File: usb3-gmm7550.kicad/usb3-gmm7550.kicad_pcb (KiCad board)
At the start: 4 copper layers, 75 x 50 mm, 205 parts, among them J1 USB_C_Receptacle, J2 USB_C_Receptacle_USB2.0, J3 SWD, J4 10144517-061802LF, J5 10144517-061802LF, J6 DNI, Q1 NX6008NBK, Q2 NX6008NBK, Q3 NX6008NBK, Q4 STL9P3LLH6, Q5 STL9P3LLH6, Q6 STL9P3LLH6, SW1 SW_Push, SW2 SW_Push, SW3 SW_Push, SW4 SW_Push, SW5 SW_Push, SW6 SW_DIP_x02, U1 ECMF4-40A100N10, U10 74LVC1G07, U11 INA180A2, U12 AP7330, U13 AP7330, U14 MX25R1635FZU, U15 ECMF02-2AMX6, U16 LM4040DBZ-3, U17 RP2040, U18 STUSB1600, U19 LM66200DRLR, U2 ECMF4-40A100N10, U3 ECMF02-2AMX6, U4 AP7330, U5 TUSB542, U6 SN65LVDS4RSER, U7 USB3340, U8 STUSB03E, U9 SiP32510, Y1 445I23D12M00000

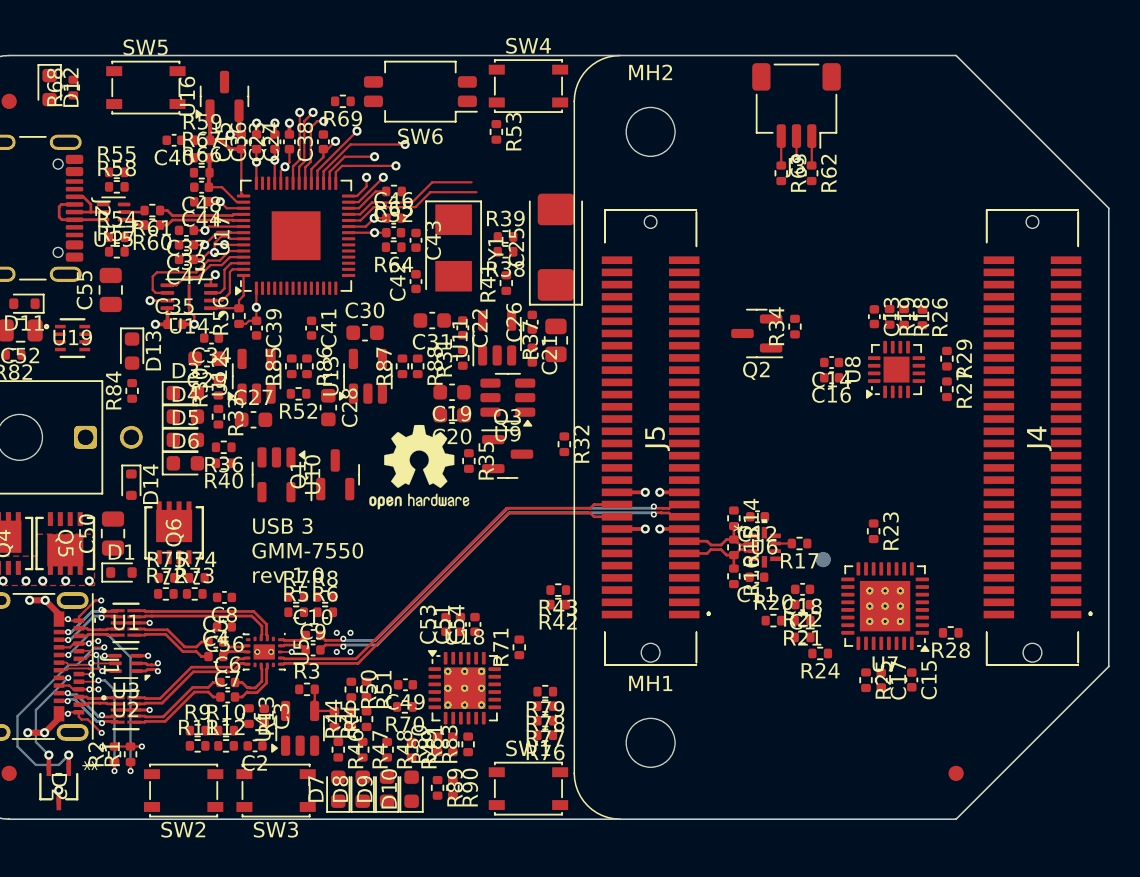
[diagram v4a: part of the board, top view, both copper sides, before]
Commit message: Layout -- suffling FPGA IOs (LEDs, buttons)
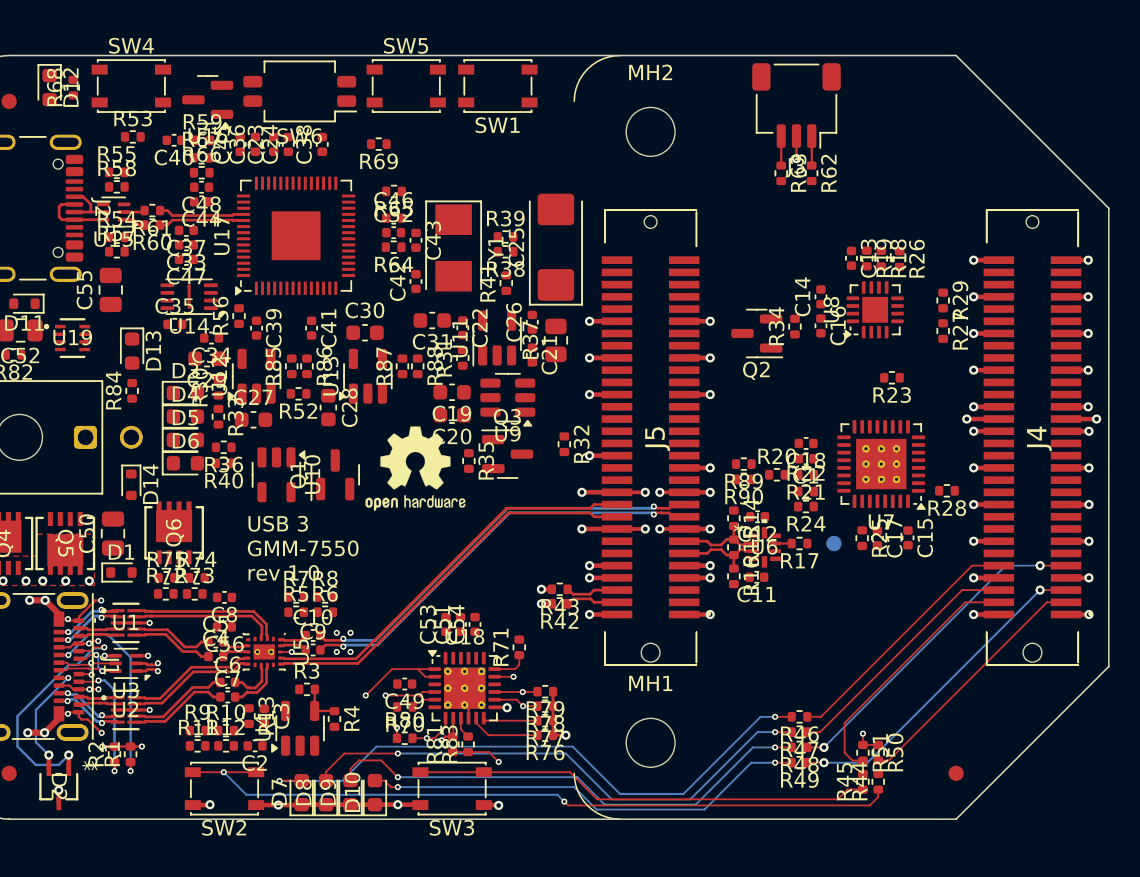
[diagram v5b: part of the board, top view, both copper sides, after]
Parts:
- moved SW1 46.0 mm to (95.0, 52.0), turned to 180 degrees
- moved R50 34.7 mm to (119.9, 95.7)
- moved R44 34.7 mm to (119.9, 97.5)
- moved R51 32.8 mm to (118.9, 95.7)
- moved R45 32.8 mm to (118.9, 97.5)
- moved R46 30.3 mm to (114.8, 93.3), turned to 180 degrees
- moved R89 29.2 mm to (111.1, 76.8), turned to 180 degrees
- moved R47 28.6 mm to (114.8, 94.3), turned to 180 degrees
- moved R90 27.8 mm to (111.1, 77.8), turned to 180 degrees
- moved R48 27.0 mm to (114.8, 95.3), turned to 180 degrees
- moved SW4 26.0 mm to (71.0, 52.0)
- moved R49 25.4 mm to (114.8, 96.3), turned to 180 degrees
- moved R53 23.8 mm to (71.1, 55.3), turned to 0 degrees
- moved SW5 17.1 mm to (89.0, 52.0)
- moved SW3 11.5 mm to (92.0, 98.0)
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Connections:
- J4 pad 10: ULPI_D7 -> /GMM-7550 IO/IO_SB_B2
- J4 pad 11: PD_RESET -> PD_SCL
- J4 pad 12: ULPI_D6 -> PD_SDA
- J4 pad 15: ULPI_D5 -> PD_ALERT_N
- J4 pad 16: ULPI_D3 -> unconnected-(J4-Pad16)
- J4 pad 17: ULPI_D4 -> unconnected-(J4-Pad17)
- J4 pad 18: ULPI_D2 -> unconnected-(J4-Pad18)
- J4 pad 28: PD_SCL -> unconnected-(J4-Pad28)
- J4 pad 3: ULPI_RST_N -> /GMM-7550 IO/IO_SB_B8
- J4 pad 30: PD_SDA -> unconnected-(J4-Pad30)
- J4 pad 38: PD_ALERT_N -> unconnected-(J4-Pad38)
- J4 pad 4: ULPI_NXT -> /GMM-7550 IO/IO_SB_B3
- J4 pad 49: /GMM-7550 IO/IO_SA_B2 -> unconnected-(J4-Pad49)
- J4 pad 5: ULPI_CLK -> /GMM-7550 IO/IO_SA_A8
- J4 pad 51: /GMM-7550 IO/IO_SA_A2 -> unconnected-(J4-Pad51)
- J4 pad 55: /GMM-7550 IO/IO_SA_B1 -> unconnected-(J4-Pad55)
- J4 pad 56: /GMM-7550 IO/IO_SA_B0 -> unconnected-(J4-Pad56)
- J4 pad 57: /GMM-7550 IO/IO_SA_A1 -> unconnected-(J4-Pad57)
- J4 pad 58: /GMM-7550 IO/IO_SA_A0 -> unconnected-(J4-Pad58)
- J4 pad 6: ULPI_DIR -> /GMM-7550 IO/IO_SB_A3
- J4 pad 9: ULPI_STP -> /GMM-7550 IO/IO_SB_B6
- R44 pad 2: /GMM-7550 IO/IO_SA_A2 -> /GMM-7550 IO/IO_SB_B8
- R45 pad 2: /GMM-7550 IO/IO_SA_B2 -> /GMM-7550 IO/IO_SB_B3
- R46 pad 1: /GMM-7550 IO/IO_SA_A0 -> /GMM-7550 IO/IO_SB_B2
- R47 pad 1: /GMM-7550 IO/IO_SA_A1 -> /GMM-7550 IO/IO_SB_A3
- R48 pad 1: /GMM-7550 IO/IO_SA_B0 -> /GMM-7550 IO/IO_SB_B6
- R49 pad 1: /GMM-7550 IO/IO_SA_B1 -> /GMM-7550 IO/IO_SA_A8
- R50 pad 2: /GMM-7550 IO/IO_SA_A2 -> /GMM-7550 IO/IO_SB_B8
- R51 pad 2: /GMM-7550 IO/IO_SA_B2 -> /GMM-7550 IO/IO_SB_B3
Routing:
- net GND: track 38.2 -> 103.2 mm, vias 30 -> 65
- net Net-(R44-Pad1): track 0.00 -> 48.6 mm, vias 0 -> 2
- net Net-(D7-A): track 0.00 -> 39.3 mm, vias 0 -> 2
- net Net-(D8-A): track 0.00 -> 34.6 mm, vias 0 -> 2
- net Net-(D9-A): track 0.00 -> 32.6 mm, vias 0 -> 2
- net Net-(R45-Pad1): track 0.00 -> 30.0 mm
- net Net-(D10-A): track 0.00 -> 29.3 mm, vias 0 -> 2
- net VIO_2V5: track 0.00 -> 23.2 mm, vias 0 -> 12
- net /GMM-7550 IO/IO_SB_B6: track 0.00 -> 21.9 mm, vias 0 -> 2
- net /GMM-7550 IO/IO_SA_A8: track 0.00 -> 21.6 mm, vias 0 -> 2
- net +2V5: track 17.2 -> 0.00 mm, vias 6 -> 0
- net /GMM-7550 IO/IO_SB_B3: track 0.00 -> 16.7 mm
- net /GMM-7550 IO/IO_SB_B2: track 0.00 -> 16.6 mm
- net /GMM-7550 IO/IO_SB_B8: track 0.00 -> 16.6 mm
- net /GMM-7550 IO/IO_SB_A3: track 0.00 -> 16.4 mm
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
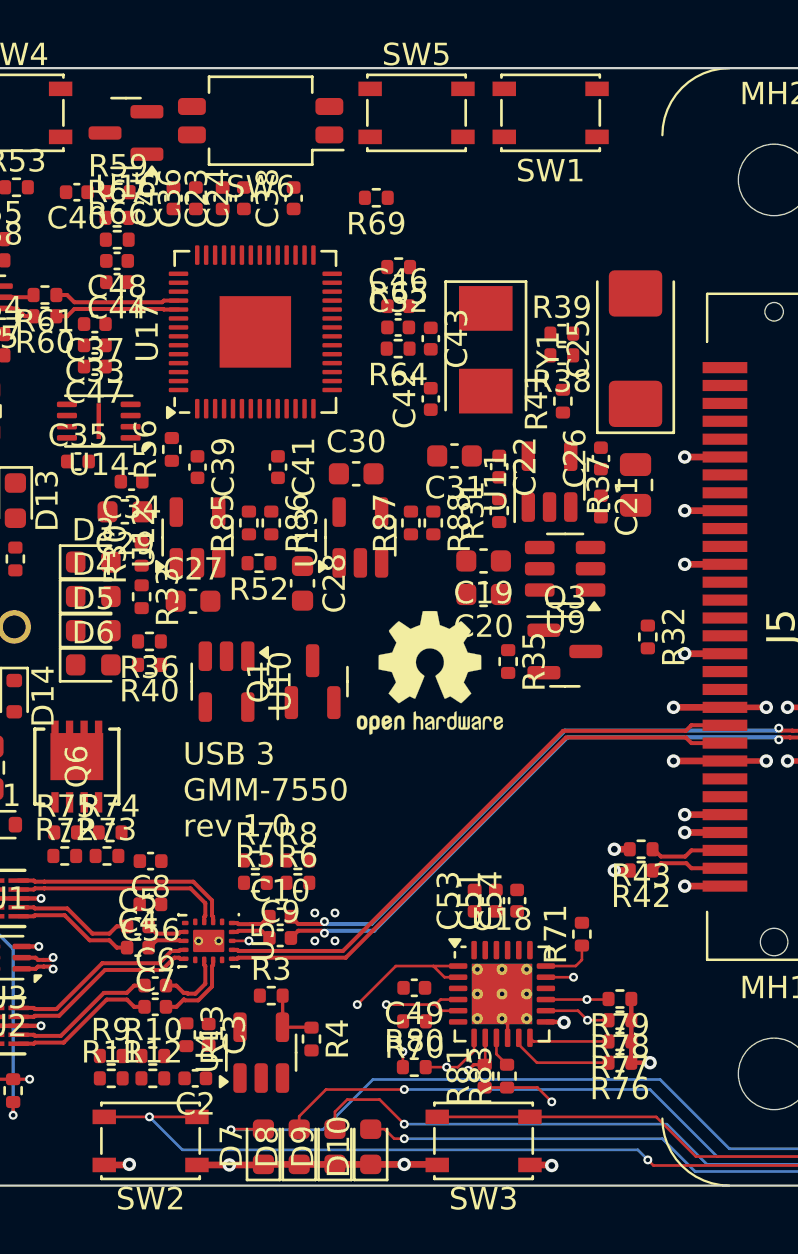
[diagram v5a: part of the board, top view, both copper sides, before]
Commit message: Add USB Type-C plug polarity indication (A_B_SIDE signal from PD controller)
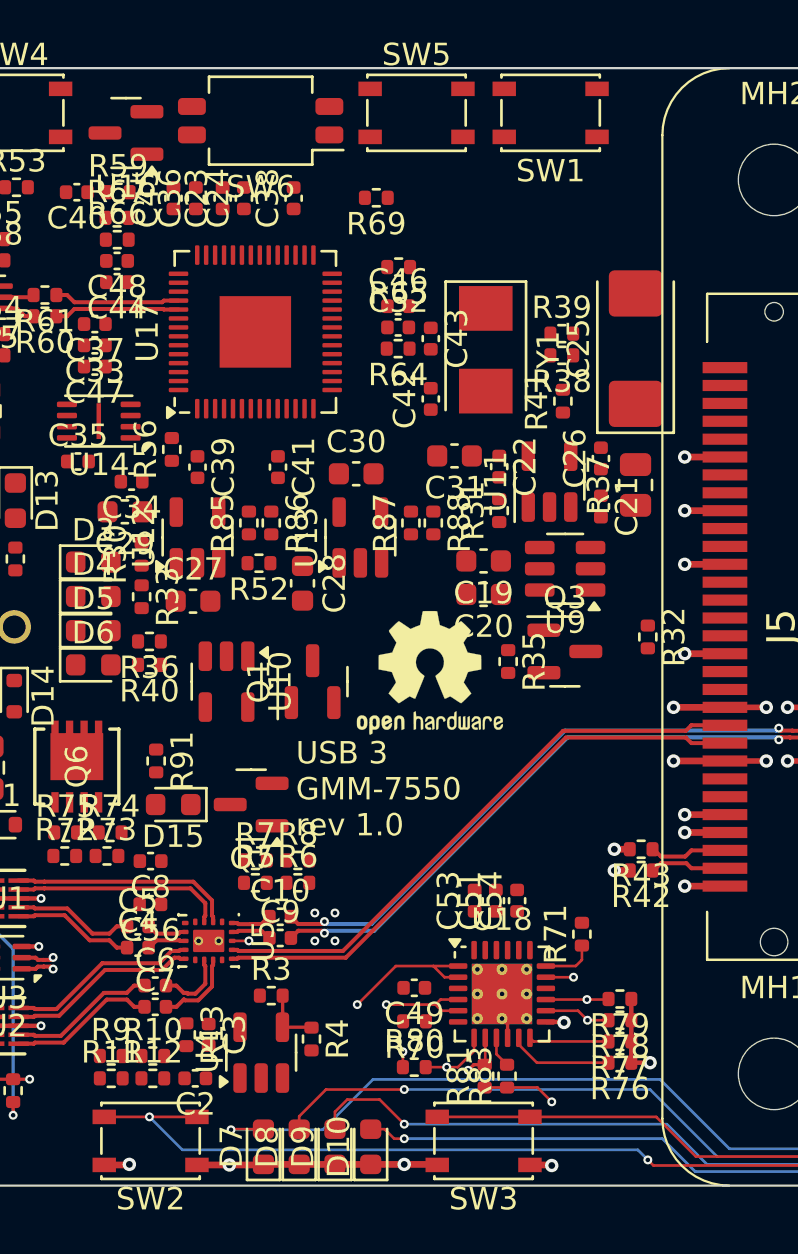
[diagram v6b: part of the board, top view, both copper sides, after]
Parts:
- added D15: HSMA-C197, LED_SMD:LED_0603_1608Metric, F.Cu at (78.1, 83.0)
- added Q7: NX6008NBK, Package_TO_SOT_SMD:SOT-23, F.Cu at (81.6, 83.0)
- added R91: 100, Resistor_SMD:R_0402_1005Metric, F.Cu at (77.3, 81.0)

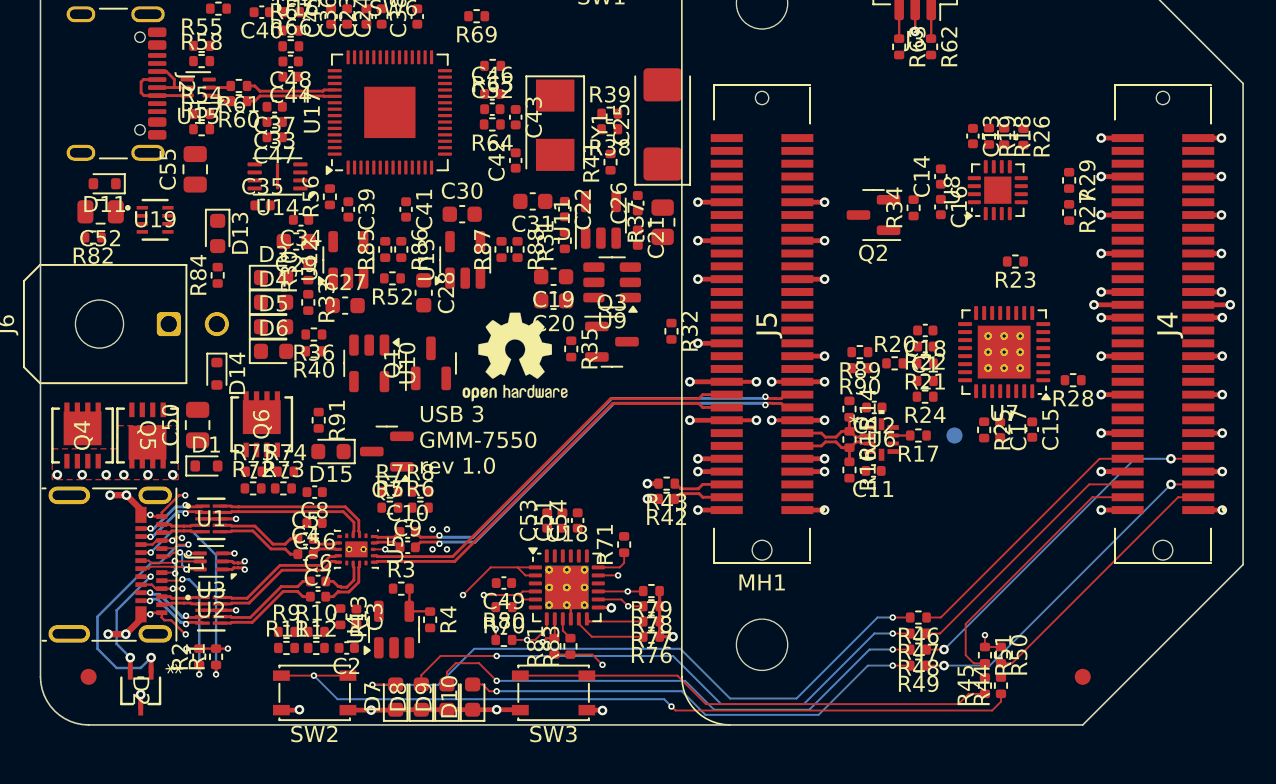
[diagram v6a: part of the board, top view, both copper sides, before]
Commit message: Layout -- re-arrange and connect all GMM-7550 IOs on J4 (USB 1.1 and 2.0)
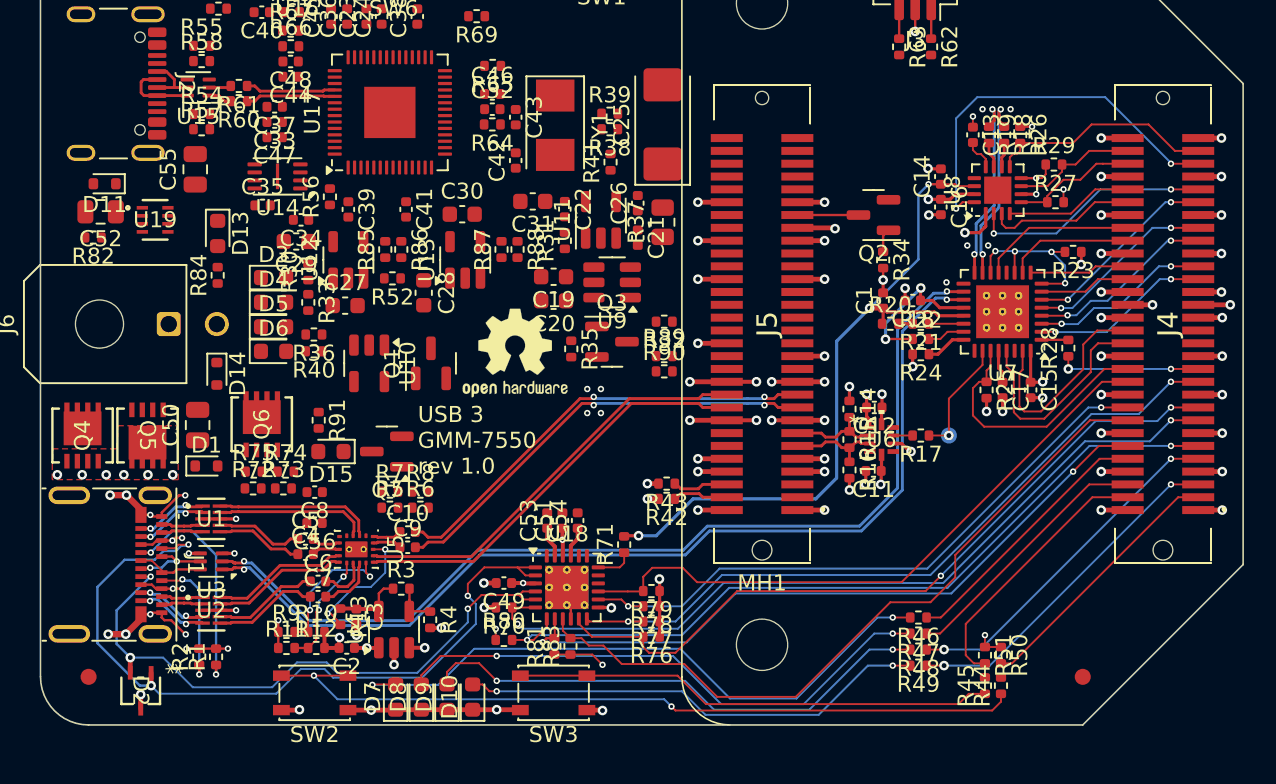
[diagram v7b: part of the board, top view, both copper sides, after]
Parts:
- moved R89 12.2 mm to (98.9, 77.0), turned to 0 degrees
- moved R90 12.2 mm to (98.9, 78.0), turned to 0 degrees
- moved C1 3.89 mm to (112.5, 73.5), turned to 90 degrees
- moved R34 3.76 mm to (112.5, 71.0), turned to -90 degrees
- moved R23 3.65 mm to (124.4, 70.5)
- moved R24 2.66 mm to (114.9, 76.9)
- moved R22 2.63 mm to (114.9, 75.9)
- moved U7 2.52 mm to (120.0, 74.2)
- moved C17 2.49 mm to (120.0, 79.1)
- moved R25 2.49 mm to (119.0, 79.1)
- moved R21 2.49 mm to (114.9, 75.0)
- moved R20 2.48 mm to (113.0, 75.0)
- moved C15 2.47 mm to (121.8, 79.1)
- moved C18 2.03 mm to (114.4, 73.5)
- moved R28 2.02 mm to (124.1, 76.5), turned to 90 degrees
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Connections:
- net /GMM-7550 IO/IO_SA_A8 renamed /GMM-7550 IO/IO_SB_A8
- J4 pad 15: PD_ALERT_N -> PD_RESET
- J4 pad 16: unconnected-(J4-Pad16) -> PD_ALERT_N
- J4 pad 17: unconnected-(J4-Pad17) -> PD_VBUS_VALID
- J4 pad 18: unconnected-(J4-Pad18) -> PD_DEBUG1
- J4 pad 21: IO_SB_B7 -> PD_ATTACH
- J4 pad 22: ULPI_D1 -> PD_DEBUG2
- J4 pad 23: IO_SB_A7 -> ULPI_CLK
- J4 pad 24: ULPI_D0 -> ULPI_RST_N
- J4 pad 27: PD_VBUS_VALID -> unconnected-(J4-Pad27)
- J4 pad 28: unconnected-(J4-Pad28) -> ULPI_STP
- J4 pad 29: PD_ATTACH -> unconnected-(J4-Pad29)
- J4 pad 30: unconnected-(J4-Pad30) -> ULPI_DIR
- J4 pad 37: USB1_BUSDET -> ULPI_NXT
- J4 pad 38: unconnected-(J4-Pad38) -> ULPI_D4
- J4 pad 39: USB1_CON -> ULPI_D0
- J4 pad 40: USB1_SUS -> ULPI_D5
- J4 pad 43: PD_DEBUG1 -> ULPI_D1
- J4 pad 44: USB1_VP -> ULPI_D6
- J4 pad 45: PD_DEBUG2 -> ULPI_D2
- J4 pad 46: USB1_VM -> ULPI_D7
- J4 pad 49: unconnected-(J4-Pad49) -> ULPI_D3
- J4 pad 50: USB1_OE_N -> USB1_VP
- J4 pad 51: unconnected-(J4-Pad51) -> USB1_RCV
- J4 pad 52: USB1_RCV -> USB1_VM
- J4 pad 55: unconnected-(J4-Pad55) -> USB1_BUSDET
- J4 pad 56: unconnected-(J4-Pad56) -> USB1_CON
- J4 pad 57: unconnected-(J4-Pad57) -> USB1_OE_N
- J4 pad 58: unconnected-(J4-Pad58) -> USB1_SUS
- U3 pad 1: USB2_D_P -> USB2_D_N
- U3 pad 2: USB2_D_N -> USB2_D_P
- U3 pad 5: /USB3/J1_D_N -> /USB3/J1_D_P
- U3 pad 6: /USB3/J1_D_P -> /USB3/J1_D_N
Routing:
- net USB2_D_P: track 1.49 -> 62.2 mm, vias 1 -> 2
- net USB2_D_N: track 1.49 -> 62.2 mm, vias 1 -> 2
- net PD_RESET: track 0.00 -> 50.6 mm, vias 0 -> 2
- net PD_SCL: track 3.05 -> 49.9 mm, vias 1 -> 2
- net VBUS_TRGT: track 5.46 -> 51.0 mm, vias 10 -> 13
- net PD_ALERT_N: track 1.40 -> 45.6 mm
- net PD_ATTACH: track 3.58 -> 45.3 mm, vias 0 -> 2
- net PD_VBUS_VALID: track 4.65 -> 46.4 mm, vias 0 -> 2
- net PD_SDA: track 2.06 -> 43.6 mm, vias 1 -> 2
- net PD_DEBUG2: track 2.85 -> 39.7 mm, vias 1 -> 0
- net PD_DEBUG1: track 2.98 -> 39.3 mm, vias 1 -> 2
- net CON_CC2: track 12.3 -> 38.5 mm
- net CON_CC1: track 22.9 -> 48.7 mm
- net USB1_BUSDET: track 0.00 -> 24.3 mm, vias 0 -> 2
- net GND: track 103.2 -> 124.4 mm, vias 65 -> 91
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
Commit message: Layout -- WIP...
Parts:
- added TP2: TestPoint, TestPoint:TestPoint_Pad_D1.0mm, B.Cu at (124.1, 77.8)
- moved C8 1.99 mm to (79.0, 84.9), turned to 0 degrees
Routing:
- net A_B_SIDE: track 8.01 -> 43.8 mm, vias 2 -> 4
- net GND: track 124.4 -> 150.9 mm, vias 91 -> 114
- net Net-(U18-VBUS_EN_SNK): track 0.00 -> 23.5 mm, vias 0 -> 2
- net Net-(U18-VBUS_EN_SRC): track 0.00 -> 23.2 mm, vias 0 -> 2
- net Net-(U11-+): track 0.00 -> 11.1 mm
- net VSW_1V8: track 6.36 -> 16.1 mm, vias 1 -> 5
- net /GMM-7550/VIN: track 0.00 -> 7.89 mm
- net Net-(U17-XIN): track 0.00 -> 7.73 mm
- net Net-(U5-CNFG_B1): track 0.00 -> 6.86 mm, vias 0 -> 2
- net VBUS_TRGT: track 51.0 -> 57.7 mm, vias 13 -> 15
- net +1V1: track 0.00 -> 6.52 mm
- net +5V: track 3.24 -> 9.60 mm, vias 2 -> 6
- net +2V5: track 0.00 -> 6.07 mm
- net Net-(C43-Pad2): track 0.00 -> 4.94 mm
- net Net-(R41-Pad1): track 0.00 -> 4.87 mm
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- added copper zone on F.Cu, net /GMM-7550/VIN
